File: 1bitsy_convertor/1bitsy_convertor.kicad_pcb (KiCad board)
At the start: 2 copper layers, 31.8 x 43.2 mm, 14 parts, among them U1 1bitsy_convertor, U2 1bitsy-complete

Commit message: Incomplete refactoring of testing points, still need to add one for the SPI CLK and positition pads on layout
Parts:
- removed REF** (x2): Measurement_Point_Round-TH_Small, Measurement_Points:Measurement_Point_Round-TH_Small
- removed REF** (x2): SDA, Measurement_Points:Measurement_Point_Round-TH_Small
- removed REF**: MOSI, Measurement_Points:Measurement_Point_Round-TH_Small
- removed REF**: MISO, Measurement_Points:Measurement_Point_Round-TH_Small
- added J1: USART_RX_TEST, Pin_Headers:Pin_Header_Straight_1x01_Pitch2.54mm, F.Cu at (171.7, 137.6)
- added J10: AIO_1_TEST, Pin_Headers:Pin_Header_Straight_1x01_Pitch2.54mm, F.Cu at (163.5, 86.4)
- added J11: I2C_SDA_TEST, Pin_Headers:Pin_Header_Straight_1x01_Pitch2.54mm, F.Cu at (104.3, 109.4)
- added J12: USART_TX_TEST, Pin_Headers:Pin_Header_Straight_1x01_Pitch2.54mm, F.Cu at (155.0, 137.7)
- added J2: SPI_MOSI_TEST, Pin_Headers:Pin_Header_Straight_1x01_Pitch2.54mm, F.Cu at (181.6, 107.4)
- added J3: I2C_SCL_TEST, Pin_Headers:Pin_Header_Straight_1x01_Pitch2.54mm, F.Cu at (115.8, 102.8)
- added J4: AIO_0_TEST, Pin_Headers:Pin_Header_Straight_1x01_Pitch2.54mm, F.Cu at (113.8, 109.4)
- added J5: AIO_2_TEST, Pin_Headers:Pin_Header_Straight_1x01_Pitch2.54mm, F.Cu at (151.4, 86.8)
- added J6: PWR_5V_TEST, Pin_Headers:Pin_Header_Straight_1x01_Pitch2.54mm, F.Cu at (103.9, 116.0)
- added J7: GND_TEST, Pin_Headers:Pin_Header_Straight_1x01_Pitch2.54mm, F.Cu at (121.2, 116.0)
- added J8: SPI_MISO_TEST, Pin_Headers:Pin_Header_Straight_1x01_Pitch2.54mm, F.Cu at (181.5, 97.1)
- added J9: AIO_3_TEST, Pin_Headers:Pin_Header_Straight_1x01_Pitch2.54mm, F.Cu at (113.2, 116.0)
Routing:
- net /SPI_MOSI: track 11.7 -> 8.16 mm
- net /I2C_SDA: track 22.0 -> 18.5 mm
- net /I2C_SCL: track 17.2 -> 13.8 mm
- net /USART_TX: track 9.00 -> 5.91 mm
- net /SPI_MISO: track 15.8 -> 13.2 mm
- net /USART_RX: track 12.7 -> 10.4 mm

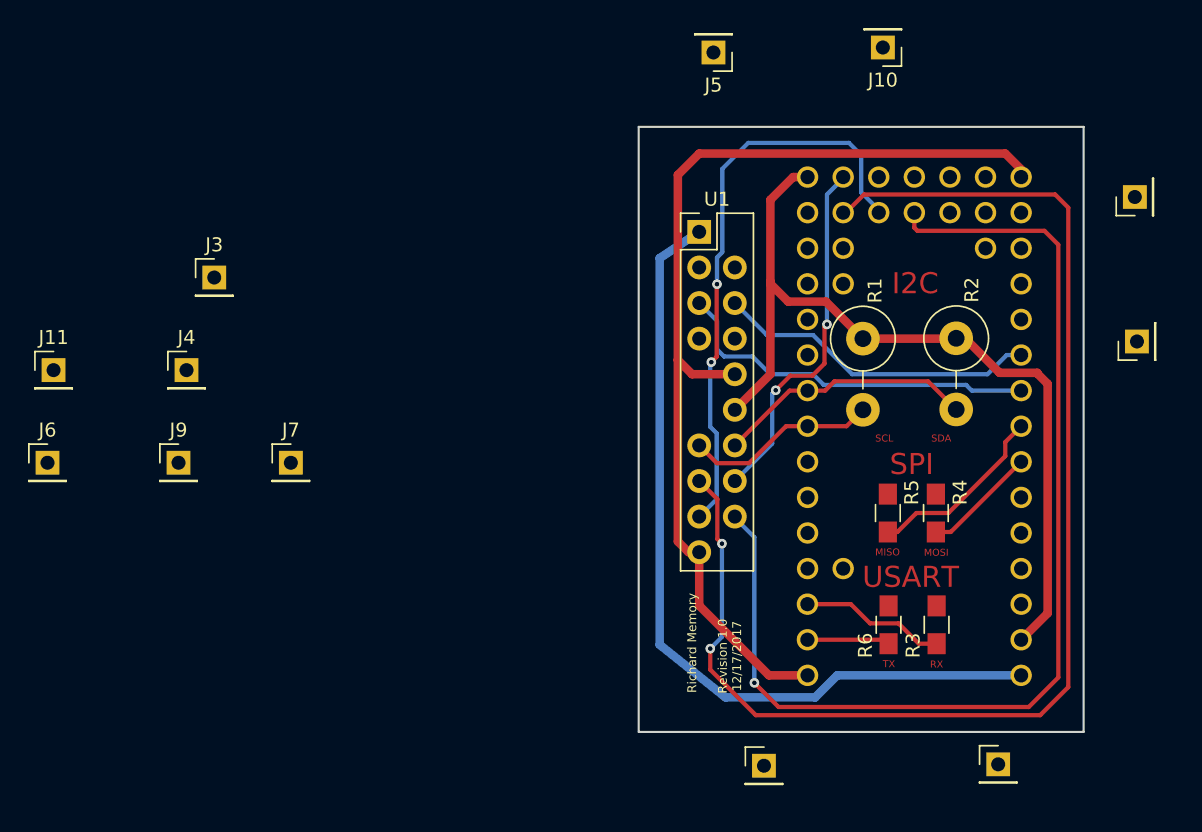
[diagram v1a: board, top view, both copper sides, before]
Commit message: layout with test points
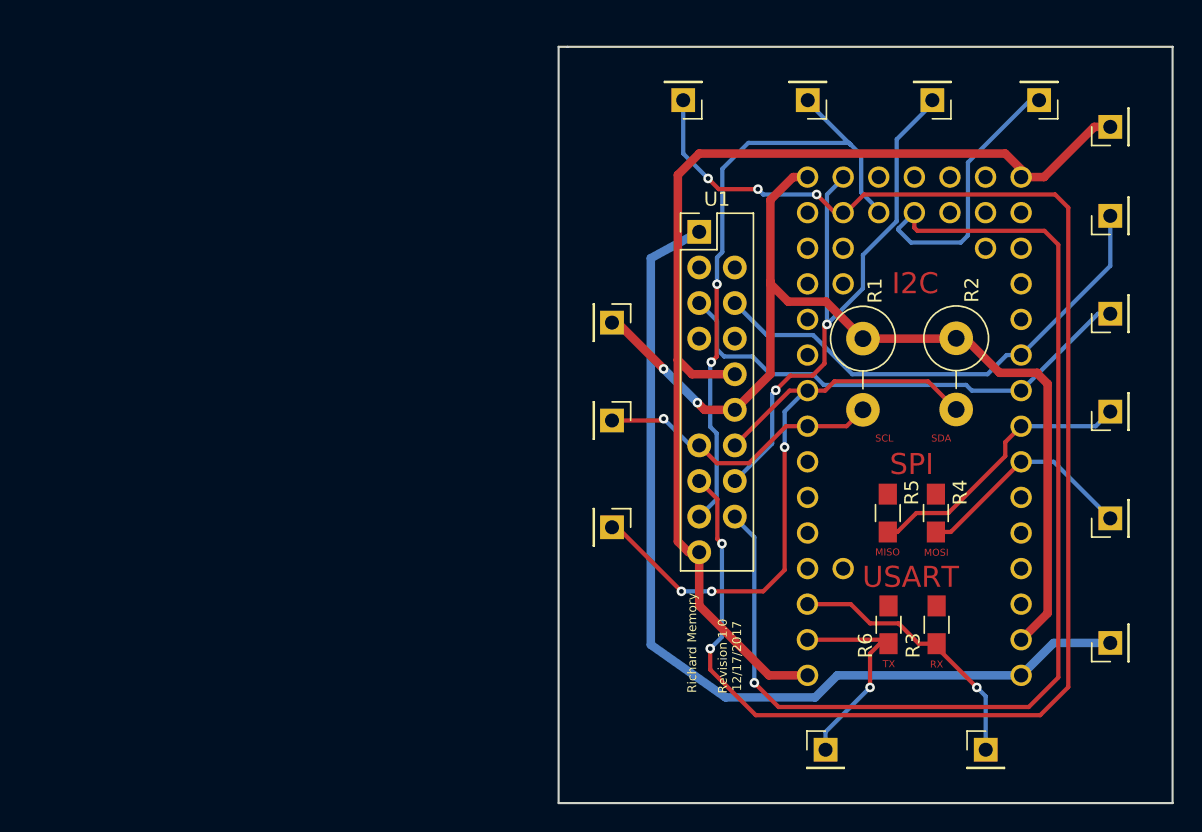
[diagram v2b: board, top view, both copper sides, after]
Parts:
- added J13: I2C_SCL, Pin_Headers:Pin_Header_Straight_1x01_Pitch2.54mm, F.Cu at (144.1, 113.0)
- added J14: USART_RX, Pin_Headers:Pin_Header_Straight_1x01_Pitch2.54mm, F.Cu at (170.8, 136.5)
- added J15: SPI_SCS, Pin_Headers:Pin_Header_Straight_1x01_Pitch2.54mm, F.Cu at (179.7, 98.4)
- J1: value USART_RX_TEST -> SPI_SCK
- J10: value AIO_1_TEST -> AIO_1
- J11: value I2C_SDA_TEST -> I2C_SDA
- J12: value USART_TX_TEST -> USART_TX
- J2: value SPI_MOSI_TEST -> SPI_MOSI
- J3: value I2C_SCL_TEST -> PWR_3.3
- J4: value AIO_0_TEST -> AIO_0
- J5: value AIO_2_TEST -> AIO_2
- J6: value PWR_5V_TEST -> PWR_5V
- J7: value GND_TEST -> GND
- J8: value SPI_MISO_TEST -> SPI_MISO
- J9: value AIO_3_TEST -> AIO_3
- moved J6 76.9 mm to (179.7, 128.9), turned to 90 degrees
- moved J9 66.6 mm to (174.6, 90.2), turned to 180 degrees
- moved J7 63.2 mm to (179.7, 92.1), turned to 90 degrees
- moved J11 41.4 mm to (144.1, 120.7), turned to 270 degrees
- moved J4 40.3 mm to (149.2, 90.2), turned to 180 degrees
- moved J1 33.1 mm to (179.7, 105.4), turned to 90 degrees
- moved J3 28.6 mm to (144.1, 106.0), turned to 270 degrees
- moved J8 15.4 mm to (179.7, 112.4)
- moved J2 12.8 mm to (179.7, 120.0)
- moved J5 7.54 mm to (158.1, 90.2)
- moved J10 5.16 mm to (167.0, 90.2)
- moved J12 4.54 mm to (159.4, 136.5)
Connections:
- J1 pad 1: /USART_RX -> /SPI_SCK
- J3 pad 1: /I2C_SCL -> /PWR_3.3
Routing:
- net /I2C_SDA: track 18.5 -> 46.9 mm, vias 0 -> 3
- net /AIO_3: track 78.5 -> 97.8 mm
- net /AIO_1: track 26.4 -> 45.5 mm
- net /AIO_0: track 93.4 -> 110.4 mm, vias 2 -> 5
- net /SPI_CS: track 23.1 -> 35.7 mm
- net /PWR_3.3: track 61.4 -> 72.7 mm, vias 0 -> 2
- net /USART_TX: track 5.91 -> 15.7 mm, vias 0 -> 1
- net /USART_RX: track 10.4 -> 19.4 mm, vias 0 -> 1
- net /SPI_SCK: track 26.8 -> 35.4 mm
- net /PWR_5: track 58.7 -> 67.1 mm
- net /SPI_MOSI: track 8.16 -> 16.2 mm
- net /GND: track 72.2 -> 80.1 mm
- net /I2C_SCL: track 13.8 -> 20.9 mm, vias 0 -> 1
- net /SPI_MISO: track 13.2 -> 20.0 mm
- net /AIO_2: track 41.5 -> 46.0 mm
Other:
- board size 31.8 x 43.2 mm -> 43.8 x 54 mm
